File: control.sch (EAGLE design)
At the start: 115 parts, among them IC1 LM358N, IC2 XMEGA16A4A, IC3 LM317MBSTT3, IC5 LM358N, Q1 BSS123, Q10 TIP42C, Q11 BC338, Q12 BC548, Q13 BC557C, Q14 BSS123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

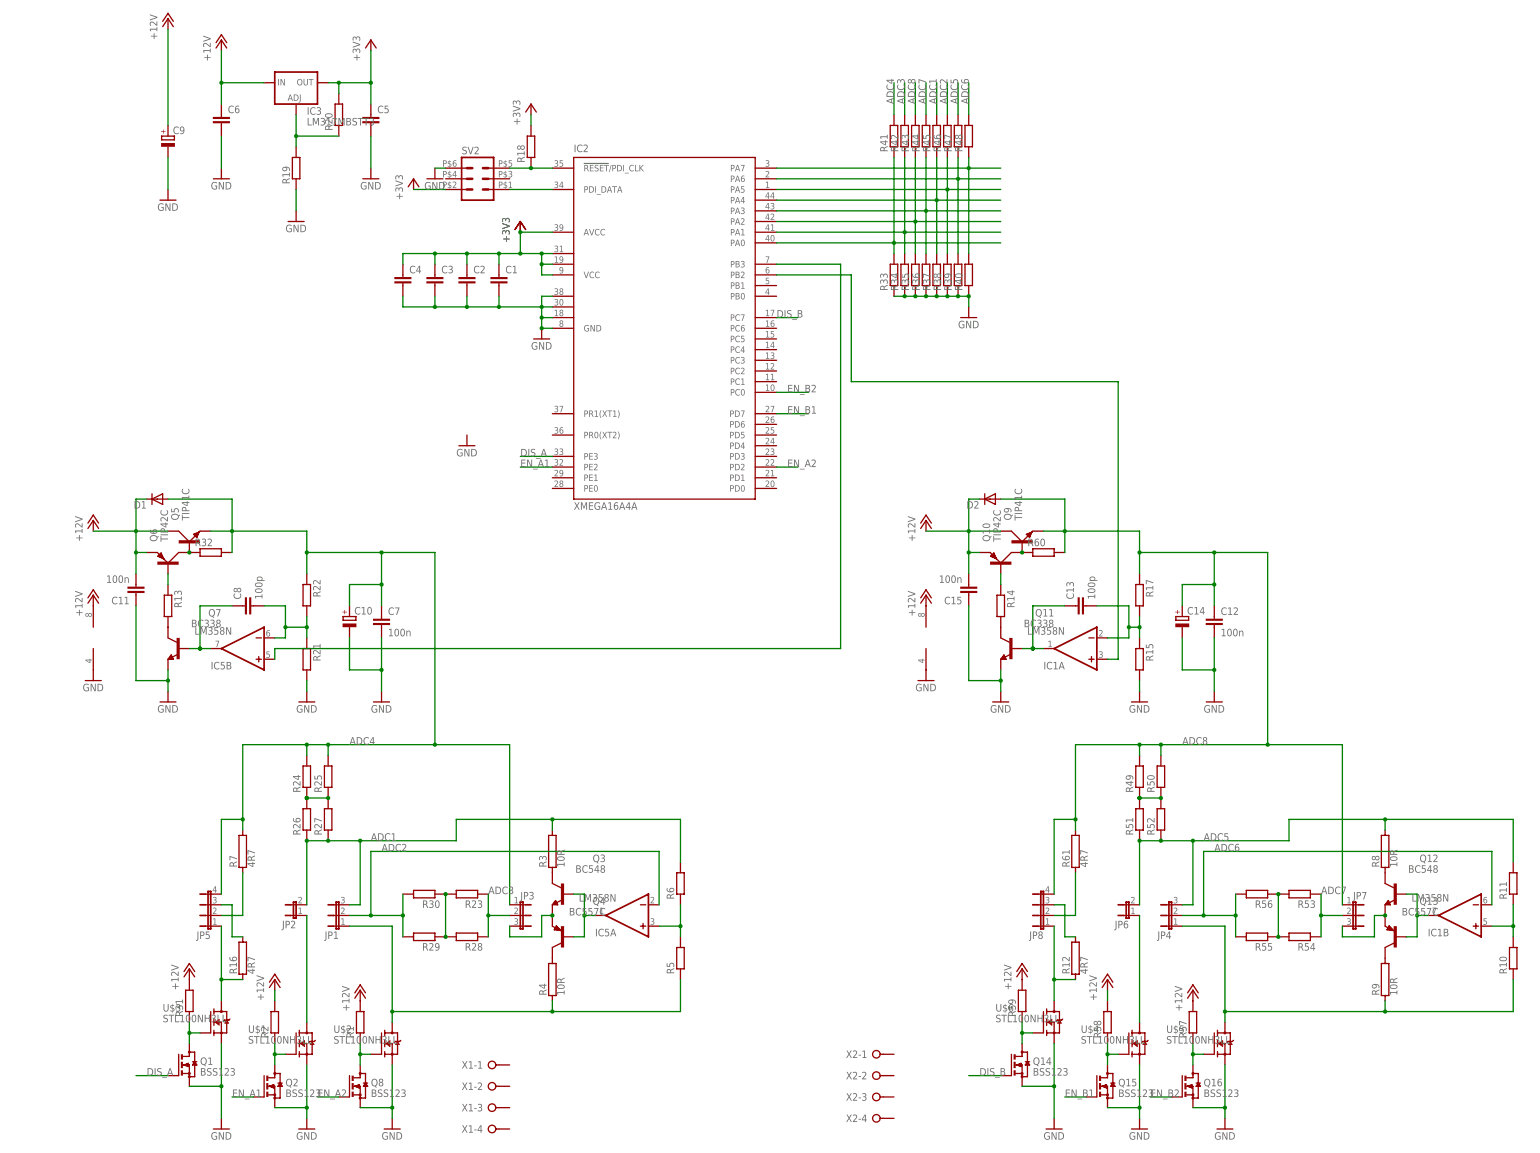
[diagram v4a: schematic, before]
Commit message: klemmen ersetzt
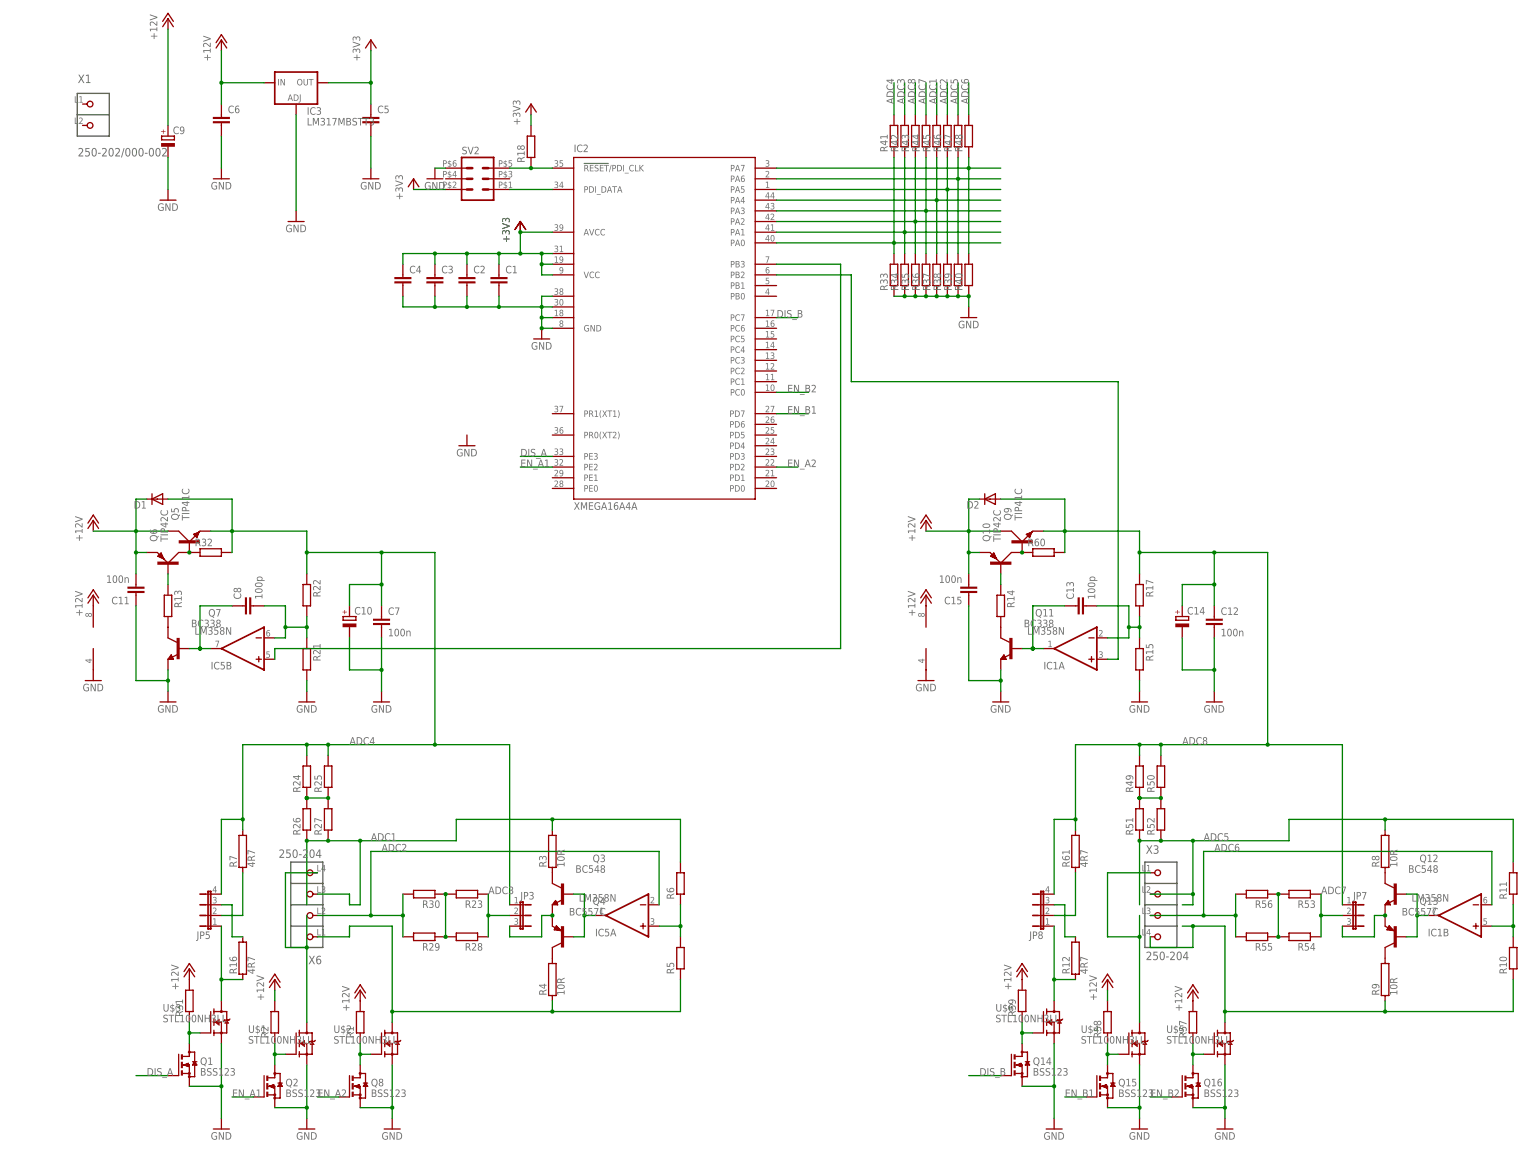
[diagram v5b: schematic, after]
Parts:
- removed JP1, JP4: (no value), jumper:JP2E
- removed JP2, JP6: (no value), jumper:JP1E
- removed R19, R20: (no value), resistor:R-EU_M0805
- removed X2: (no value), con-wago-508:W237-04P
- added X3, X6: 250-204, con-wago_250:250-204
- X1: value (none) -> 250-202/000-002; device con-wago-508:W237-04P -> con-wago_250:250-202/000-002
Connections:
- removed net N$27: IC3.ADJ, R19.2, R20.1
- net +3V3: no longer R20.2
- net ADC1: now also X6.P3; no longer JP1.3, JP2.2
- net ADC2: now also X6.P2; no longer JP1.2
- net ADC5: now also X3.P2; no longer JP4.3, JP6.2
- net ADC6: now also X3.P3; no longer JP4.2
- net GND: now also IC3.ADJ; no longer R19.1
- net N$1: now also X6.P1; no longer JP1.1
- net N$2: now also X3.P4; no longer JP4.1
- net N$3: now also X3.P1; no longer JP6.1
- net N$4: now also X6.P4; no longer JP2.1

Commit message: routing
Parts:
- C1, C2, C3, C4, C5, C6: value (none) -> 100n
- C10, C14, C9: value (none) -> 100µ
- R1, R15, R18, R2, R21, R31, R33, R34, R35, R36, R37, R38, R39, R40, R57, R58, R59: value (none) -> 10k
- R10, R11, R17, R22, R41, R42, R43, R44, R45, R46, R47, R48, R5, R6: value (none) -> 33k
- R13, R14, R32, R60: value (none) -> 330
- R23, R24, R25, R26, R27, R28, R29, R30, R49, R50, R51, R52, R53, R54, R55, R56: value (none) -> 1
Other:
- moved on the sheet: Q1, Q14, R21, R31, R59, U$3, U$6, X6

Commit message: GND polygon, schaltplan aufräumen
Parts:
- removed C5: 100n, resistor:C-EUC0805K
- added JP1: (no value), jumper:JP2E
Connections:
- new net N$27: IC2.PC3, JP1.1
- new net N$38: IC2.PC2, JP1.2
- net +12V: now also X1.P2
- net +3V3: no longer C5.1
- net DIS_B: now also IC2.PC1; no longer IC2.PC7
- net EN_A2: now also IC2.PE0; no longer IC2.PD2
- net EN_B1: now also IC2.PC4; no longer IC2.PD7
- net EN_B2: now also IC2.PC5; no longer IC2.PC0
- net GND: now also JP1.3, X1.P1; no longer C5.2
- net N$31: now also IC2.PB2; no longer IC2.PB3
- net N$48: now also IC2.PB3; no longer IC2.PB2
- net N$55: now also U$4.G; no longer U$6.G
- net N$56: now also U$6.G; no longer U$4.G
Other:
- moved on the sheet: Q14, Q15, R58, R59, X1

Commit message: LEDs
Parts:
- added LED1, LED2, LED3, LED4: (no value), led:LEDCHIPLED_0805
- added R19, R20, R62, R63: 33k, resistor:R-EU_M0805
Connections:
- new net N$10: IC2.PD1, R20.1
- new net N$39: IC2.PD2, R62.1
- new net N$5: IC2.PD0, R19.1
- new net N$58: IC2.PD3, R63.1
- new net N$59: LED4.A, R63.2
- new net N$60: LED3.A, R62.2
- new net N$61: LED2.A, R20.2
- new net N$62: LED1.A, R19.2
- net GND: now also LED1.C, LED2.C, LED3.C, LED4.C
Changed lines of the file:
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@@
 <part name="JP1" library="jumper" deviceset="JP2E" device=""/>
 <part name="GND23" library="supply1" deviceset="GND" device=""/>
+<part name="LED1" library="led" deviceset="LED" device="CHIPLED_0805"/>
+<part name="LED2" library="led" deviceset="LED" device="CHIPLED_0805"/>
+<part name="LED3" library="led" deviceset="LED" device="CHIPLED_0805"/>
+<part name="LED4" library="led" deviceset="LED" device="CHIPLED_0805"/>
+<part name="R19" library="resistor" deviceset="R-EU_" device="M0805" value="33k"/>
+<part name="R20" library="resistor" deviceset="R-EU_" device="M0805" value="33k"/>
+<part name="R62" library="resistor" deviceset="R-EU_" device="M0805" value="33k"/>
+<part name="R63" library="resistor" deviceset="R-EU_" device="M0805" value="33k"/>
+<part name="GND9" library="supply1" deviceset="GND" device=""/>
 </parts>
 <sheets>
@@
 <instance part="JP1" gate="1" x="172.72" y="187.96" rot="R270"/>
 <instance part="GND23" gate="1" x="170.18" y="182.88"/>
+<instance part="LED1" gate="G$1" x="177.8" y="160.02" rot="R90"/>
+<instance part="LED2" gate="G$1" x="177.8" y="162.56" rot="R90"/>
+<instance part="LED3" gate="G$1" x="177.8" y="165.1" rot="R90"/>
+<instance part="LED4" gate="G$1" x="177.8" y="167.64" rot="R90"/>
+<instance part="R19" gate="G$1" x="165.1" y="160.02"/>
+<instance part="R20" gate="G$1" x="165.1" y="162.56"/>
+<instance part="R62" gate="G$1" x="165.1" y="165.1"/>
+<instance part="R63" gate="G$1" x="165.1" y="167.64"/>
+<instance part="GND9" gate="1" x="187.96" y="154.94"/>
 </instances>
 <busses>
@@
 <pinref part="JP1" gate="1" pin="3"/>
 <pinref part="GND23" gate="1" pin="GND"/>
+</segment>
+<segment>
+<pinref part="GND9" gate="1" pin="GND"/>
+<wire x1="187.96" y1="167.64" x2="187.96" y2="165.1" width="0.1524" layer="91"/>
+<pinref part="LED1" gate="G$1" pin="C"/>
+<wire x1="187.96" y1="165.1" x2="187.96" y2="162.56" width="0.1524" layer="91"/>
+<wire x1="187.96" y1="162.56" x2="187.96" y2="160.02" width="0.1524" layer="91"/>
+<wire x1="187.96" y1="160.02" x2="187.96" y2="157.48" width="0.1524" layer="91"/>
+<wire x1="182.88" y1="160.02" x2="187.96" y2="160.02" width="0.1524" layer="91"/>
+<junction x="187.96" y="160.02"/>
+<pinref part="LED2" gate="G$1" pin="C"/>
+<wire x1="187.96" y1="162.56" x2="182.88" y2="162.56" width="0.1524" layer="91"/>
+<junction x="187.96" y="162.56"/>
+<pinref part="LED3" gate="G$1" pin="C"/>
+<wire x1="182.88" y1="165.1" x2="187.96" y2="165.1" width="0.1524" layer="91"/>
+<junction x="187.96" y="165.1"/>
+<pinref part="LED4" gate="G$1" pin="C"/>
+<wire x1="187.96" y1="167.64" x2="182.88" y2="167.64" width="0.1524" layer="91"/>
 </segment>
 </net>
@@
 </segment>
 </net>
+<net name="N$5" class="0">
+<segment>
+<pinref part="IC2" gate="G$1" pin="PD0"/>
+<pinref part="R19" gate="G$1" pin="1"/>
+<wire x1="160.02" y1="160.02" x2="157.48" y2="160.02" width="0.1524" layer="91"/>
+</segment>
+</net>
+<net name="N$10" class="0">
+<segment>
+<pinref part="IC2" gate="G$1" pin="PD1"/>
+<pinref part="R20" gate="G$1" pin="1"/>
+<wire x1="160.02" y1="162.56" x2="157.48" y2="162.56" width="0.1524" layer="91"/>
+</segment>
+</net>
+<net name="N$39" class="0">
+<segment>
+<pinref part="IC2" gate="G$1" pin="PD2"/>
+<pinref part="R62" gate="G$1" pin="1"/>
+<wire x1="160.02" y1="165.1" x2="157.48" y2="165.1" width="0.1524" layer="91"/>
+</segment>
+</net>
+<net name="N$58" class="0">
+<segment>
+<pinref part="IC2" gate="G$1" pin="PD3"/>
+<pinref part="R63" gate="G$1" pin="1"/>
+<wire x1="160.02" y1="167.64" x2="157.48" y2="167.64" width="0.1524" layer="91"/>
+</segment>
+</net>
+<net name="N$59" class="0">
+<segment>
+<pinref part="R63" gate="G$1" pin="2"/>
+<pinref part="LED4" gate="G$1" pin="A"/>
+<wire x1="170.18" y1="167.64" x2="175.26" y2="167.64" width="0.1524" layer="91"/>
+</segment>
+</net>
+<net name="N$60" class="0">
+<segment>
+<pinref part="LED3" gate="G$1" pin="A"/>
+<pinref part="R62" gate="G$1" pin="2"/>
+<wire x1="175.26" y1="165.1" x2="170.18" y2="165.1" width="0.1524" layer="91"/>
+</segment>
+</net>
+<net name="N$61" class="0">
+<segment>
+<pinref part="R20" gate="G$1" pin="2"/>
+<pinref part="LED2" gate="G$1" pin="A"/>
+<wire x1="170.18" y1="162.56" x2="175.26" y2="162.56" width="0.1524" layer="91"/>
+</segment>
+</net>
+<net name="N$62" class="0">
+<segment>
+<pinref part="LED1" gate="G$1" pin="A"/>
+<pinref part="R19" gate="G$1" pin="2"/>
+<wire x1="175.26" y1="160.02" x2="170.18" y2="160.02" width="0.1524" layer="91"/>
+</segment>
+</net>
